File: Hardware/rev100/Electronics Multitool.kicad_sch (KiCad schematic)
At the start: 0 parts

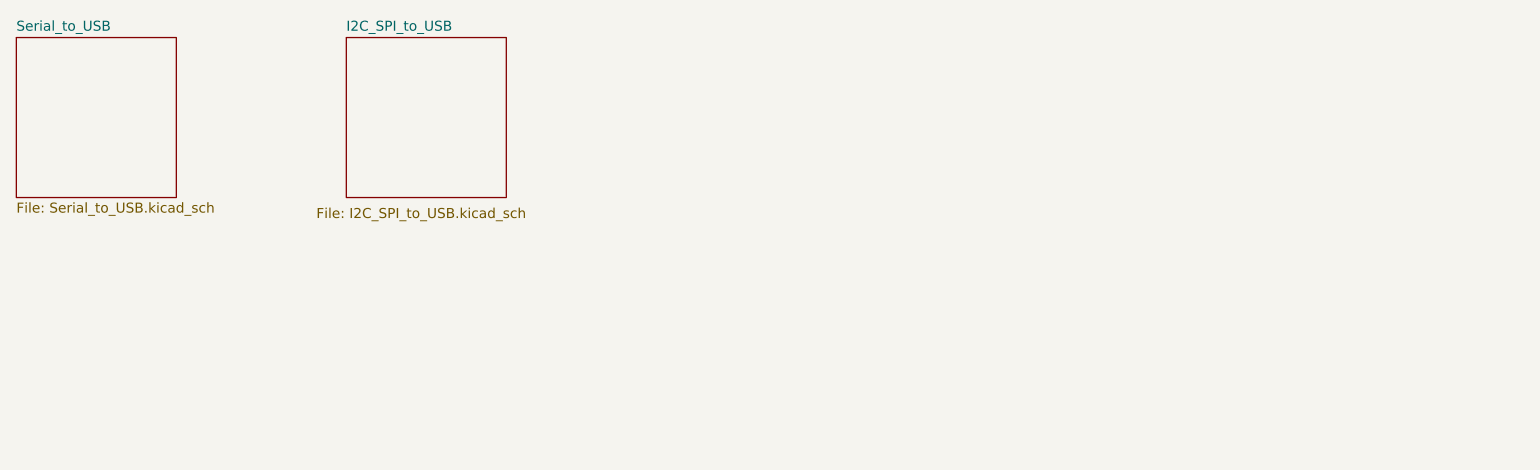
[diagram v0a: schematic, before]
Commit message: Included USB ports on schematic
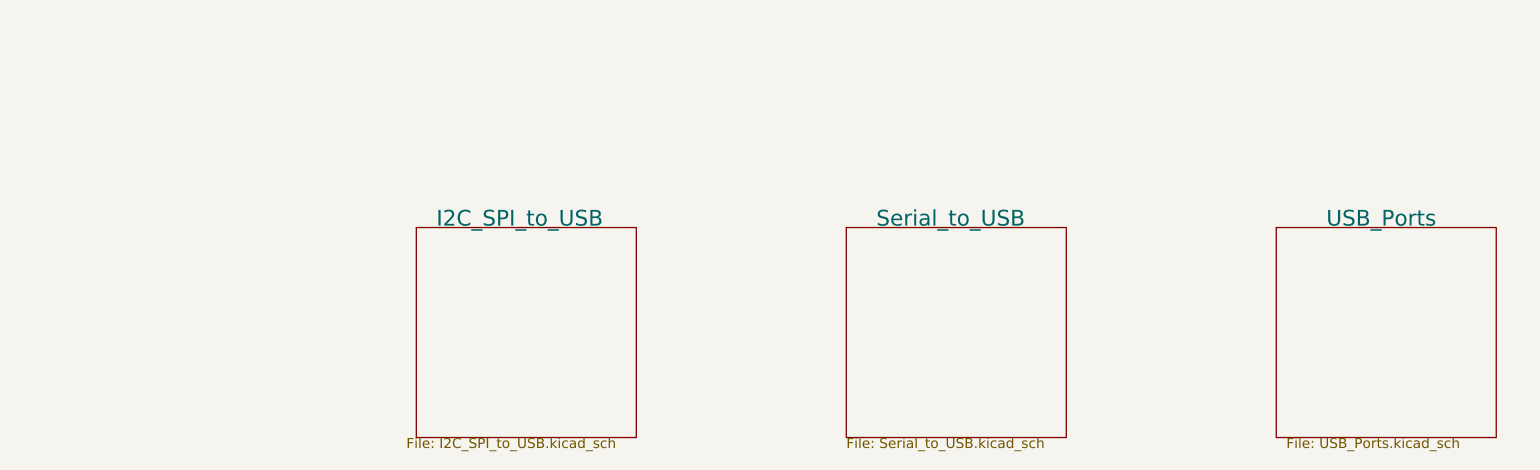
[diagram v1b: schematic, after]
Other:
- added sheet USB_Ports (USB_Ports.kicad_sch)
